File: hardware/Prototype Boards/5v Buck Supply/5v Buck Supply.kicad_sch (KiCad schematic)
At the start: 3 parts, among them J1 BATT, U1 INA180A1IDBVT

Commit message: sync hardware work
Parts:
- removed U1: INA180A1IDBVT, INA180A1IDBVT:SOT95P280X145-5N, symbol project_symbols:INA180A1IDBVT
- added BAT_CON1: BAT, symbol Connector:Screw_Terminal_01x03
- added BT1, BT2: INR21700-50E, symbol Device:Battery_Cell
- added C1, C2: DNS, Capacitor_SMD:C_1210_3225Metric, symbol Device:C
- added C10: 75pf, Capacitor_SMD:C_0603_1608Metric_Pad1.08x0.95mm_HandSolder, symbol Device:C
- added C11, C15: 1uf, Capacitor_SMD:C_0805_2012Metric, symbol Device:C
- added C12, C14: DNS, Capacitor_SMD:C_1210_3225Metric_Pad1.33x2.70mm_HandSolder, symbol Device:C
- added C13, C4, C5: 0.1uf, Capacitor_SMD:C_0603_1608Metric_Pad1.08x0.95mm_HandSolder, symbol Device:C
- added C3: 10uf, Capacitor_SMD:C_1210_3225Metric, symbol Device:C
- added C6, C7: C, Capacitor_SMD:C_0603_1608Metric_Pad1.08x0.95mm_HandSolder, symbol Device:C_Small
- added C8, C9: 22uf, Capacitor_SMD:C_1210_3225Metric, symbol Device:C
- added D1, D2: BAT54S, Package_TO_SOT_SMD:SOT-23, symbol Device:D_Dual_Series_ACK
- added J2: Switch Current, Connector_PinSocket_2.54mm:PinSocket_1x02_P2.54mm_Vertical, symbol Connector_Generic:Conn_01x02
- added J3: SW, Connector_PinSocket_2.54mm:PinSocket_1x01_P2.54mm_Vertical, symbol Connector_Generic:Conn_01x01
- added J4: OUT, Connector_PinSocket_2.54mm:PinSocket_1x01_P2.54mm_Vertical, symbol Connector_Generic:Conn_01x01
- added J5: PRIMARY, TerminalBlock_TE-Connectivity:TerminalBlock_TE_282834-3_1x03_P2.54mm_Horizontal, symbol Connector:Screw_Terminal_01x03
- added J6: EXTERNAL, TerminalBlock_TE-Connectivity:TerminalBlock_TE_282834-2_1x02_P2.54mm_Horizontal, symbol Connector:Screw_Terminal_01x02
- added J7: IO, Connector_PinHeader_2.54mm:PinHeader_1x10_P2.54mm_Vertical, symbol Connector:Conn_01x10_Socket
- added J8: 5v Primary, Connector_PinSocket_2.54mm:PinSocket_1x02_P2.54mm_Vertical, symbol Connector_Generic:Conn_01x02
- added J9: 3v3 Primary, Connector_PinSocket_2.54mm:PinSocket_1x02_P2.54mm_Vertical, symbol Connector_Generic:Conn_01x02
- added L1: 10uH, footprints:IND_SRU1048-100Y, symbol Device:L
- added Q1: NPN, Package_TO_SOT_SMD:SOT-23, symbol Simulation_SPICE:NPN
- added R10, R11, R12, R13, R14, R15, R17, R19, R21, R3, R4, R5, R6, R7, R8, R9: R, Capacitor_SMD:C_0603_1608Metric_Pad1.08x0.95mm_HandSolder, symbol Device:R_Small
- added R16, R18, R20, R27, R28: R_Shunt, Resistor_SMD:R_0805_2012Metric_Pad1.20x1.40mm_HandSolder, symbol Device:R_Shunt
- added R2: DNS, Resistor_SMD:R_0603_1608Metric_Pad0.98x0.95mm_HandSolder, symbol Device:R
- added R22: 49.9k, Resistor_SMD:R_0603_1608Metric_Pad0.98x0.95mm_HandSolder, symbol Device:R
- added R23: 100k, Resistor_SMD:R_0603_1608Metric_Pad0.98x0.95mm_HandSolder, symbol Device:R
- added R24: 13.3k, Resistor_SMD:R_0603_1608Metric_Pad0.98x0.95mm_HandSolder, symbol Device:R
- added R25, R26: R, Capacitor_SMD:C_0603_1608Metric_Pad1.08x0.95mm_HandSolder, symbol Device:R
- added TP1, TP10, TP11, TP12, TP2, TP5, TP6, TP7, TP8, TP9: TestPoint, footprints:KEYSTONE_5015, symbol Connector:TestPoint
- added TP3, TP4: ~, TestPoint:TestPoint_Pad_D1.5mm, symbol Connector:TestPoint_Small
- added U1: TPS54302DDCR, TPS54302DDCR:SOT95P280X110-6N, symbol project_symbols:TPS54302DDCR
- added U2: INA2180Ax, INA2180A1IDGKR:SOP65P490X110-8N, symbol project_symbols:INA2180A1IDGKR
- added U3: AP2112K-3.3, Package_TO_SOT_SMD:SOT-23-5, symbol Regulator_Linear:AP2112K-3.3
- J1: footprint (none) -> TerminalBlock_TE-Connectivity:TerminalBlock_TE_282834-3_1x03_P2.54mm_Horizontal
- R1: value ? -> DNS; footprint (none) -> Resistor_SMD:R_0603_1608Metric_Pad0.98x0.95mm_HandSolder; now not fitted
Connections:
- net +BATT: now also J1.3 (Pin_3), BAT_CON1.3 (Pin_3), BT1.1 (+), R16.1, R8.1; no longer R1.2
- net GND: now reaches R1.1
- net GND: now also J1.1 (Pin_1), BAT_CON1.1 (Pin_1), BT2.2 (-), C1.2, C11.2, C12.2, C13.2, C14.2, C15.2, C2.2, C3.2, C4.2, C8.2, C9.2, D1.1 (A), D2.1 (A), J5.1 (Pin_1), J6.1 (Pin_1), J7.1 (Pin_1), Q1.3 (E), R10.2, R11.2, R12.2, R13.2, R14.2, R24.2, R9.2, U1.1 (GND), U2.4 (GND), U3.2 (GND)
- net batt_ballance: now reaches J1.2 (Pin_2)
- net batt_ballance: now also BAT_CON1.2 (Pin_2), BT1.2 (-), BT2.1 (+), R7.1
- new net: Q1.1 (C), R25.1, U3.3 (EN)
- new net: Q1.2 (B), R26.1
- new net: C6.2, R15.2, TP6.1, U2.3 (IN+1)
- new net: C7.2, R19.2, TP10.1, U2.5 (IN+2)
- new net: J9.1 (Pin_1), R28.2
- new net: J9.2 (Pin_2), R28.3
- new net: R19.1, R20.2, TP9.1
- new net: R20.3, R21.1, TP11.1
- new net: C5.2, R18.1, U1.2 (SW)
- new net: J2.1 (Pin_1), R18.2
- new net: J2.2 (Pin_2), R18.3
- new net: J3.1 (Pin_1), L1.2, R18.4
- new net: R16.3, R17.1, TP7.1
- new net: C6.1, R17.2, TP8.1, U2.2 (IN-1)
- new net: C7.1, R21.2, TP12.1, U2.6 (IN-2)
- new net: C12.1, C14.1, C8.1, C9.1, J4.1 (Pin_1), L1.1, R22.1, R27.1
- new net: R15.1, R16.2, TP5.1
- new net: C15.1, R28.1, U3.5 (VOUT)
- new net: C5.1, TP3.1, U1.6 (BOOT)
- new net: C10.1, R22.2, R23.1
- new net: J8.1 (Pin_1), R27.2
- new net: J8.2 (Pin_2), R27.3
- new net +BATT External: J6.2 (Pin_2), R20.4
- new net +BATT Primary: C1.1, C2.1, C3.1, C4.1, R16.4, R2.2, R20.1, TP2.1, U1.3 (VIN)
- new net 3V3 Primary: C13.1, D1.3 (K), D2.3 (K), J5.2 (Pin_2), J7.3 (Pin_3), R28.4, R5.1, U2.8 (VS)
- new net 3V3_DISABLE: J7.4 (Pin_4), R26.2
- new net 5V Primary: C11.1, J5.3 (Pin_3), J7.2 (Pin_2), R25.2, R27.4, R6.1, U3.1 (VIN)
- new net adc_scaled:3V3: J7.8 (Pin_8), R11.1, R5.2
- new net adc_scaled:5V: J7.7 (Pin_7), R12.1, R6.2
- new net adc_scaled:batt: J7.5 (Pin_5), R14.1, R8.2
- new net adc_scaled:batt_ballance: J7.6 (Pin_6), R13.1, R7.2
- new net adc_scaled:current_batt: J7.9 (Pin_9), R10.1, R4.2
- new net adc_scaled:current_external: J7.10 (Pin_10), R3.2, R9.1
- new net buck_enable: R1.2, R2.1, TP1.1, U1.5 (EN)
- new net buck_feedback: C10.2, R23.2, R24.1, TP4.1, U1.4 (FB)
- new net current_sense_batt: D1.2 (common), R4.1, U2.1 (OUT1)
- new net current_sense_external: D2.2 (common), R3.1, U2.7 (OUT2)
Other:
- note added: "3V3 Primary"
- note added: "5v Primary"
- note added: "Battery"
- note added: "Current Sense"
- note added: "Shunt for debugging. Do not need this in the future."
- title: (none) -> Prototype Buck Converter
- moved on the sheet: J1

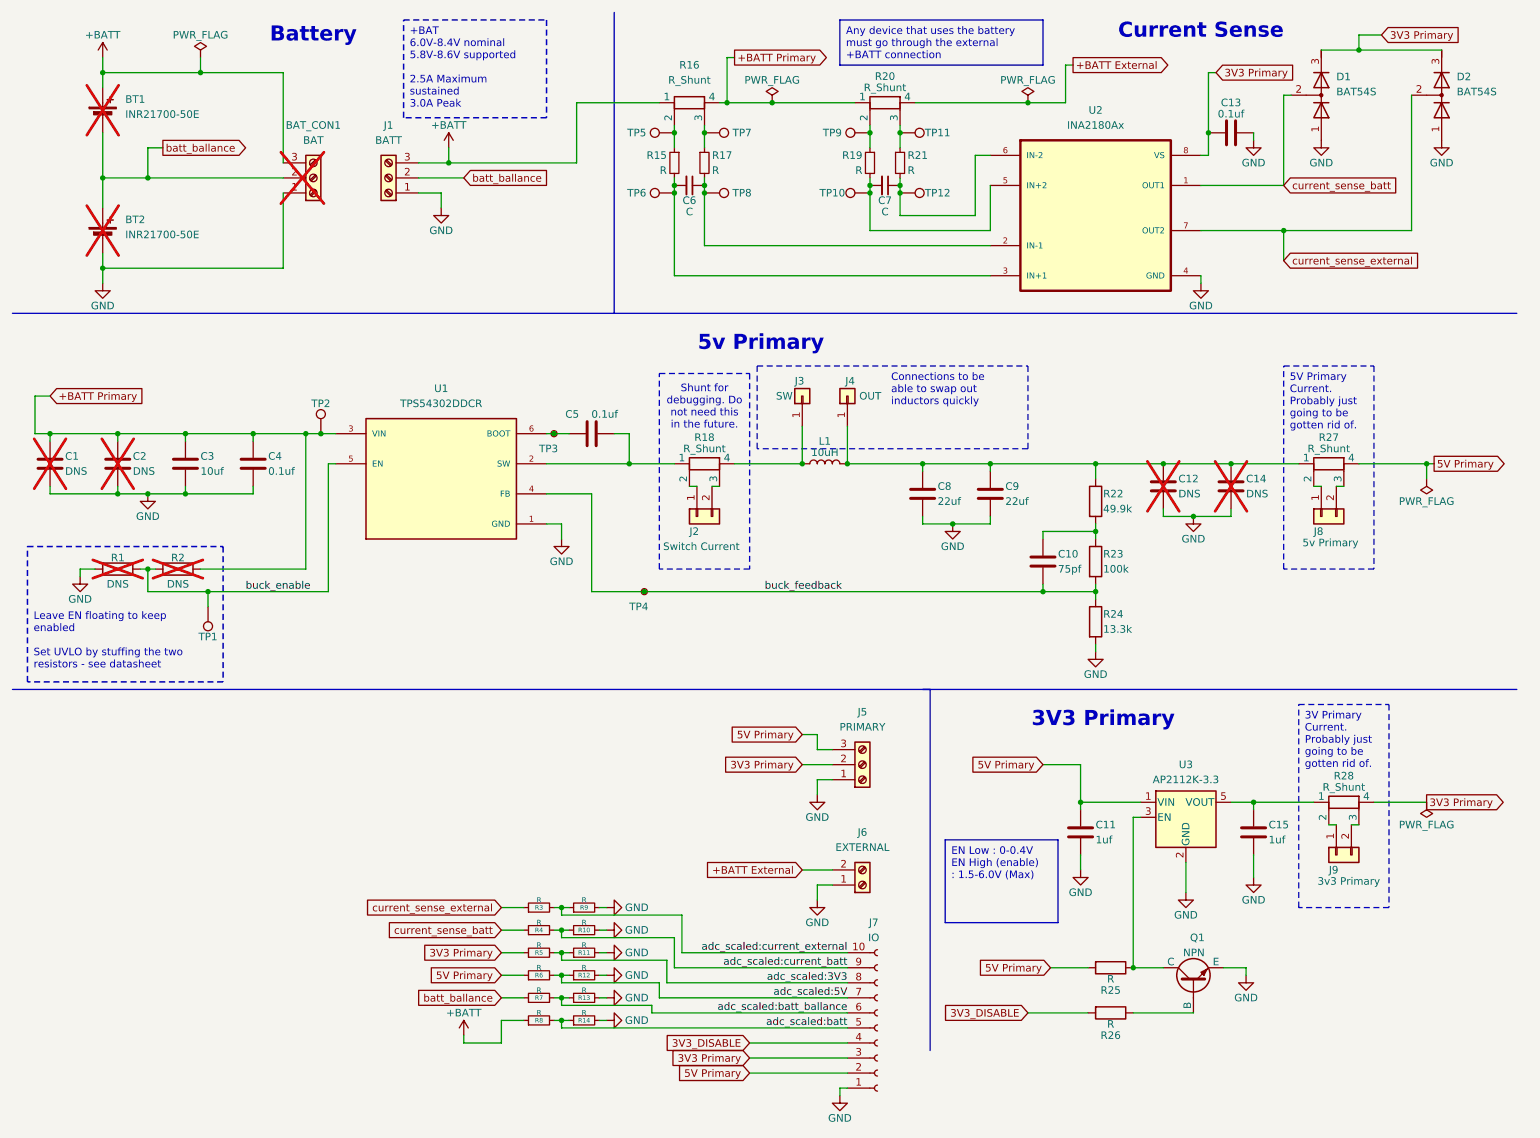
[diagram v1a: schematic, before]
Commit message: v2 buck supply
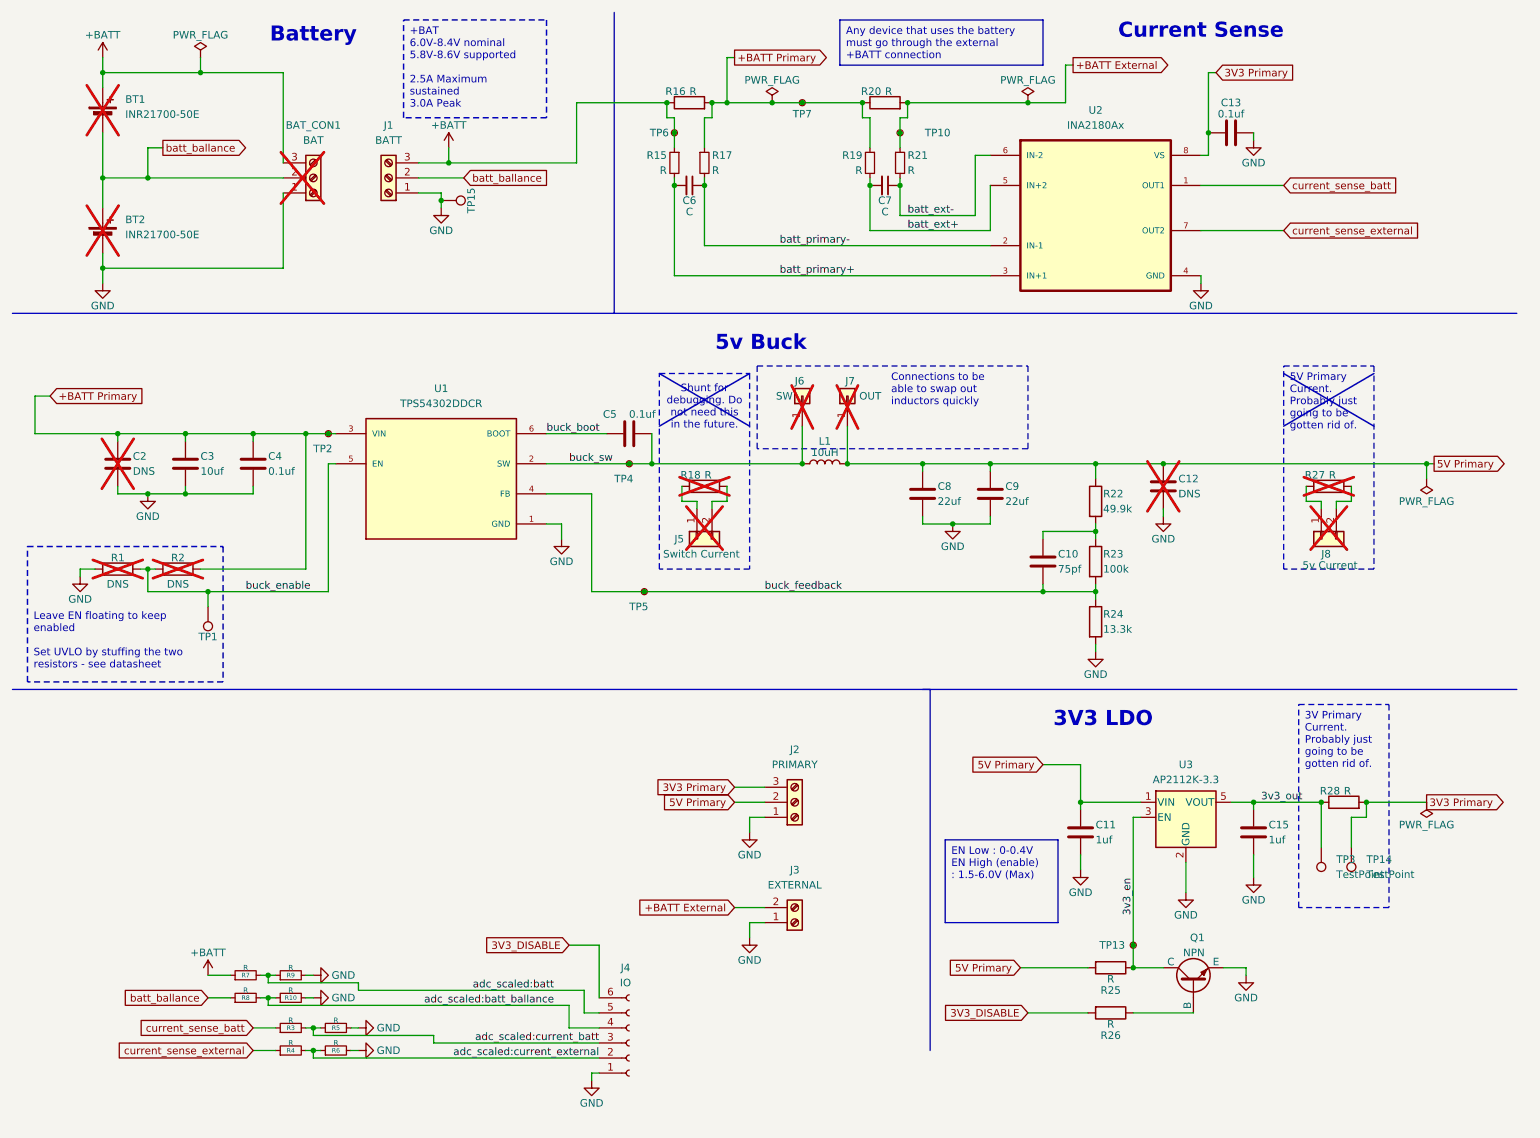
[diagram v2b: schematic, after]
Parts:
- removed C1: DNS, Capacitor_SMD:C_1210_3225Metric, symbol Device:C
- removed C14: DNS, Capacitor_SMD:C_1210_3225Metric_Pad1.33x2.70mm_HandSolder, symbol Device:C
- removed D1, D2: BAT54S, Package_TO_SOT_SMD:SOT-23, symbol Device:D_Dual_Series_ACK
- removed J2: Switch Current, Connector_PinSocket_2.54mm:PinSocket_1x02_P2.54mm_Vertical, symbol Connector_Generic:Conn_01x02
- removed J7: IO, Connector_PinHeader_2.54mm:PinHeader_1x10_P2.54mm_Vertical, symbol Connector:Conn_01x10_Socket
- removed J9: 3v3 Primary, Connector_PinSocket_2.54mm:PinSocket_1x02_P2.54mm_Vertical, symbol Connector_Generic:Conn_01x02
- removed R11, R12, R13, R14: R, Capacitor_SMD:C_0603_1608Metric_Pad1.08x0.95mm_HandSolder, symbol Device:R_Small
- removed R16, R18, R20, R27, R28: R_Shunt, Resistor_SMD:R_0805_2012Metric_Pad1.20x1.40mm_HandSolder, symbol Device:R_Shunt
- removed TP10, TP12, TP2, TP6, TP7, TP8, TP9: TestPoint, footprints:KEYSTONE_5015, symbol Connector:TestPoint
- removed TP3: ~, TestPoint:TestPoint_Pad_D1.5mm, symbol Connector:TestPoint_Small
- added J4: IO, Connector_PinHeader_2.54mm:PinHeader_1x06_P2.54mm_Vertical, symbol Connector:Conn_01x06_Socket
- added J5: Switch Current, Connector_PinSocket_2.54mm:PinSocket_1x02_P2.54mm_Vertical, symbol Connector_Generic:Conn_01x02
- added R16, R20, R28: R, Resistor_SMD:R_0805_2012Metric_Pad1.20x1.40mm_HandSolder, symbol Device:R
- added R18, R27: R, Resistor_SMD:R_0603_1608Metric_Pad0.98x0.95mm_HandSolder, symbol Device:R
- added TP13, TP2, TP4: ~, TestPoint:TestPoint_Pad_D1.0mm, symbol Connector:TestPoint_Small
- added TP14, TP15, TP3: TestPoint, footprints:KEYSTONE_5015, symbol Connector:TestPoint
- added TP7: TestPoint, TestPoint:TestPoint_Pad_D1.0mm, symbol Connector:TestPoint_Small
- C2: footprint Capacitor_SMD:C_1210_3225Metric -> Capacitor_SMD:C_1210_3225Metric_Pad1.33x2.70mm_HandSolder
- J6: renamed from J3; footprint Connector_PinSocket_2.54mm:PinSocket_1x01_P2.54mm_Vertical -> TestPoint:TestPoint_Pad_2.0x2.0mm; now not fitted; now left out of the parts list
- J7: renamed from J4; footprint Connector_PinSocket_2.54mm:PinSocket_1x01_P2.54mm_Vertical -> TestPoint:TestPoint_Pad_2.0x2.0mm; now not fitted; now left out of the parts list
- J8: value 5v Primary -> 5v Current; now not fitted; now left out of the parts list
- TP1: footprint footprints:KEYSTONE_5015 -> TestPoint:TestPoint_Pad_D1.0mm
- TP10: renamed from TP11; footprint footprints:KEYSTONE_5015 -> TestPoint:TestPoint_Pad_D1.0mm; symbol Connector:TestPoint -> Connector:TestPoint_Small
- TP5: renamed from TP4; footprint TestPoint:TestPoint_Pad_D1.5mm -> TestPoint:TestPoint_Pad_D1.0mm
- TP6: renamed from TP5; footprint footprints:KEYSTONE_5015 -> TestPoint:TestPoint_Pad_D1.0mm; symbol Connector:TestPoint -> Connector:TestPoint_Small
- U1: footprint TPS54302DDCR:SOT95P280X110-6N -> footprints:SOT95P280X110-6N
- U2: footprint INA2180A1IDGKR:SOP65P490X110-8N -> footprints:SOP65P490X110-8N
- renumbered J5 to J2, J6 to J3
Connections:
- net adc_scaled:3V3 is gone; now on net GND: R5.2
- net adc_scaled:5V is gone; now on net GND: R6.2
- net +BATT: now also R15.1, R7.1, TP6.1, R16.1; no longer R8.1
- net +BATT External: now also R21.1, TP10.1, R20.2
- net +BATT Primary: now also R17.1, R19.1, R16.2, R20.1, TP2.1, TP7.1
- net 3V3 Primary: now also J2.3 (Pin_3), R28.2, TP14.1; no longer J2.2 (Pin_2), R5.1
- net 3V3_DISABLE: now also J4.6 (Pin_6)
- net 5V Primary: now also C12.1, C8.1, C9.1, J2.2 (Pin_2), J7.1 (Pin_1), L1.1, R22.1; no longer J2.3 (Pin_3), R6.1
- net GND: now also J4.1 (Pin_1), TP15.1
- net adc_scaled:batt: now also R7.2, R9.1, J4.5 (Pin_5); no longer R8.2
- net adc_scaled:batt_ballance: now also R10.1, R8.2, J4.4 (Pin_4); no longer R7.2
- net adc_scaled:current_batt: now also R3.2, R5.1, J4.3 (Pin_3); no longer R10.1, R4.2
- net adc_scaled:current_external: now also R4.2, R6.1, J4.2 (Pin_2); no longer R3.2, R9.1
- net batt_ballance: now also R8.1; no longer R7.1
- net current_sense_batt: now also R3.1; no longer R4.1
- net current_sense_external: now also R4.1; no longer R3.1
- net 3v3_en: now reaches Q1.1 (C), R25.1, U3.3 (EN)
- net 3v3_en: now also TP13.1
- net batt_primary+: now reaches C6.2, R15.2, U2.3 (IN+1)
- net batt_ext+: now reaches C7.2, R19.2, U2.5 (IN+2)
- net buck_sw: now reaches C5.2, U1.2 (SW)
- net buck_sw: now also J6.1 (Pin_1), L1.2, TP4.1
- net batt_primary-: now reaches C6.1, R17.2, U2.2 (IN-1)
- net batt_ext-: now reaches C7.1, R21.2, U2.6 (IN-2)
- net 3v3_out: now reaches C15.1, U3.5 (VOUT)
- net 3v3_out: now also R28.1, TP3.1
- net buck_boot: now reaches C5.1, U1.6 (BOOT)
- net at J8.1 (Pin_1): now also R27.1
- net at J8.2 (Pin_2): now also R27.2
- new net: J5.1 (Pin_1), R18.1
- new net: J5.2 (Pin_2), R18.2
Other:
- note added: "3V3 LDO"
- note added: "5v Buck"
- note removed: "3V3 Primary"
- note removed: "5v Primary"
- moved on the sheet: C5, J2, J3

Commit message: buck BOM
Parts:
- C6, C7: value C -> DNS; now not fitted
- Q1: value NPN -> MMBT3904LT1G
- R10, R25, R9: value R -> 10k
- R15, R17, R19, R21, R28, R3, R4: value R -> 0
- R16, R20: value R -> 0.05
- R18, R27: value R -> DNS
- R26: value R -> 1k
- R5, R6: value R -> DNS; now not fitted
- R7: value R -> 18k
- R8: value R -> 3.3k
- TP13, TP2, TP4, TP5: value ~ -> TestPoint
- TP14, TP15, TP3: value TestPoint -> TestPoint ks
- U2: value INA2180Ax -> INA2180A2
